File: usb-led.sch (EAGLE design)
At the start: 10 parts, among them U1 Tiny85-20-SMT

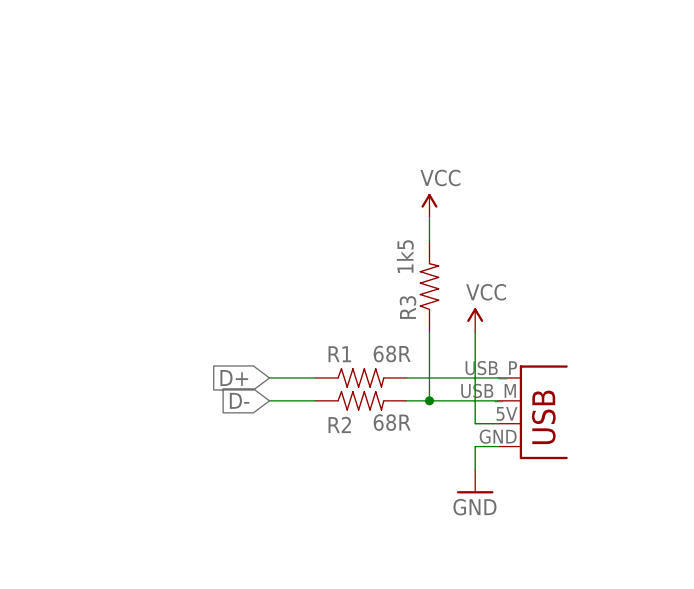
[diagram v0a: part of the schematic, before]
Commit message: Forgot two 3.6V Z-Diodes
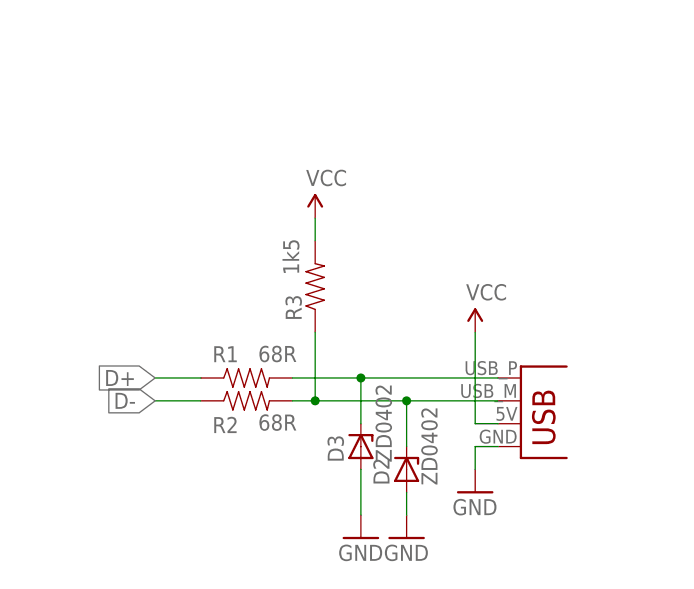
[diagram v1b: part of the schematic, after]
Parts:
- added D2, D3: ZD0402, z-diode-0402:ZD0402
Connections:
- net GND: now also D2.A, D3.A
- net N$1: now also D3.C
- net N$2: now also D2.C
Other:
- moved on the sheet: R1, R2, R3
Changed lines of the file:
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@@
 <part name="SUPPLY5" library="SparkFun-Aesthetics" deviceset="VCC" device=""/>
 <part name="R5" library="SparkFun-Passives" deviceset="RESISTOR" device="0402-RES" value="10K"/>
+<part name="D2" library="z-diode-0402" deviceset="ZD0402" device=""/>
+<part name="D3" library="z-diode-0402" deviceset="ZD0402" device=""/>
+<part name="GND4" library="SparkFun-Aesthetics" deviceset="GND" device=""/>
+<part name="GND5" library="SparkFun-Aesthetics" deviceset="GND" device=""/>
 </parts>
 <sheets>
@@
 <instance part="U1" gate="G$1" x="114.3" y="111.76"/>
 <instance part="FRAME1" gate="G$1" x="0" y="0"/>
-<instance part="R1" gate="G$1" x="129.54" y="53.34" smashed="yes">
-<attribute name="NAME" x="125.73" y="55.0926" size="1.778" layer="95"/>
-<attribute name="VALUE" x="130.81" y="55.118" size="1.778" layer="96"/>
+<instance part="R1" gate="G$1" x="116.84" y="53.34" smashed="yes">
+<attribute name="NAME" x="113.03" y="55.0926" size="1.778" layer="95"/>
+<attribute name="VALUE" x="118.11" y="55.118" size="1.778" layer="96"/>
 </instance>
-<instance part="R2" gate="G$1" x="129.54" y="50.8" smashed="yes">
-<attribute name="NAME" x="125.73" y="47.2186" size="1.778" layer="95"/>
-<attribute name="VALUE" x="130.81" y="47.498" size="1.778" layer="96"/>
+<instance part="R2" gate="G$1" x="116.84" y="50.8" smashed="yes">
+<attribute name="NAME" x="113.03" y="47.2186" size="1.778" layer="95"/>
+<attribute name="VALUE" x="118.11" y="47.498" size="1.778" layer="96"/>
 </instance>
-<instance part="R3" gate="G$1" x="137.16" y="63.5" smashed="yes" rot="R90">
-<attribute name="NAME" x="135.6614" y="59.69" size="1.778" layer="95" rot="R90"/>
-<attribute name="VALUE" x="135.382" y="64.77" size="1.778" layer="96" rot="R90"/>
+<instance part="R3" gate="G$1" x="124.46" y="63.5" smashed="yes" rot="R90">
+<attribute name="NAME" x="122.9614" y="59.69" size="1.778" layer="95" rot="R90"/>
+<attribute name="VALUE" x="122.682" y="64.77" size="1.778" layer="96" rot="R90"/>
 </instance>
 <instance part="SUPPLY1" gate="G$1" x="142.24" y="58.42"/>
@@
 <instance part="SUPPLY2" gate="G$1" x="93.98" y="121.92"/>
 <instance part="GND2" gate="1" x="93.98" y="101.6"/>
-<instance part="SUPPLY4" gate="G$1" x="137.16" y="71.12"/>
+<instance part="SUPPLY4" gate="G$1" x="124.46" y="71.12"/>
 <instance part="C1" gate="G$1" x="93.98" y="111.76"/>
 <instance part="GND3" gate="1" x="210.82" y="106.68"/>
@@
 <attribute name="VALUE" x="140.97" y="104.902" size="1.778" layer="96" rot="R180"/>
 </instance>
+<instance part="D2" gate="1" x="134.62" y="43.18" rot="R90"/>
+<instance part="D3" gate="1" x="129.54" y="45.72" rot="R90"/>
+<instance part="GND4" gate="1" x="134.62" y="35.56"/>
+<instance part="GND5" gate="1" x="129.54" y="35.56"/>
 </instances>
 <busses>
@@
 <pinref part="GND3" gate="1" pin="GND"/>
 </segment>
+<segment>
+<pinref part="D2" gate="1" pin="A"/>
+<wire x1="134.62" y1="40.64" x2="134.62" y2="38.1" width="0.1524" layer="91"/>
+<pinref part="GND4" gate="1" pin="GND"/>
+</segment>
+<segment>
+<pinref part="D3" gate="1" pin="A"/>
+<wire x1="129.54" y1="43.18" x2="129.54" y2="38.1" width="0.1524" layer="91"/>
+<pinref part="GND5" gate="1" pin="GND"/>
+</segment>
 </net>
 <net name="VCC" class="0">
@@
 <pinref part="R3" gate="G$1" pin="2"/>
 <pinref part="SUPPLY4" gate="G$1" pin="VCC"/>
-<wire x1="137.16" y1="71.12" x2="137.16" y2="68.58" width="0.1524" layer="91"/>
+<wire x1="124.46" y1="71.12" x2="124.46" y2="68.58" width="0.1524" layer="91"/>
 </segment>
 <segment>
@@
 <pinref part="R1" gate="G$1" pin="2"/>
 <pinref part="JP1" gate="G$1" pin="D+"/>
-<wire x1="134.62" y1="53.34" x2="144.78" y2="53.34" width="0.1524" layer="91"/>
+<wire x1="121.92" y1="53.34" x2="129.54" y2="53.34" width="0.1524" layer="91"/>
+<pinref part="D3" gate="1" pin="C"/>
+<wire x1="129.54" y1="53.34" x2="144.78" y2="53.34" width="0.1524" layer="91"/>
+<wire x1="129.54" y1="48.26" x2="129.54" y2="53.34" width="0.1524" layer="91"/>
+<junction x="129.54" y="53.34"/>
 </segment>
 </net>
@@
 <pinref part="JP1" gate="G$1" pin="D-"/>
 <pinref part="R2" gate="G$1" pin="2"/>
-<wire x1="144.78" y1="50.8" x2="137.16" y2="50.8" width="0.1524" layer="91"/>
+<wire x1="144.78" y1="50.8" x2="134.62" y2="50.8" width="0.1524" layer="91"/>
 <pinref part="R3" gate="G$1" pin="1"/>
-<wire x1="137.16" y1="50.8" x2="134.62" y2="50.8" width="0.1524" layer="91"/>
-<wire x1="137.16" y1="58.42" x2="137.16" y2="50.8" width="0.1524" layer="91"/>
-<junction x="137.16" y="50.8"/>
+<wire x1="134.62" y1="50.8" x2="124.46" y2="50.8" width="0.1524" layer="91"/>
+<wire x1="124.46" y1="50.8" x2="121.92" y2="50.8" width="0.1524" layer="91"/>
+<wire x1="124.46" y1="58.42" x2="124.46" y2="50.8" width="0.1524" layer="91"/>
+<junction x="124.46" y="50.8"/>
+<pinref part="D2" gate="1" pin="C"/>
+<wire x1="134.62" y1="45.72" x2="134.62" y2="50.8" width="0.1524" layer="91"/>
+<junction x="134.62" y="50.8"/>
 </segment>
 </net>
@@
 <segment>
 <pinref part="R2" gate="G$1" pin="1"/>
-<wire x1="124.46" y1="50.8" x2="119.38" y2="50.8" width="0.1524" layer="91"/>
-<label x="119.38" y="50.8" size="1.778" layer="95" rot="R180" xref="yes"/>
+<wire x1="111.76" y1="50.8" x2="106.68" y2="50.8" width="0.1524" layer="91"/>
+<label x="106.68" y="50.8" size="1.778" layer="95" rot="R180" xref="yes"/>
 </segment>
 <segment>
@@
 <segment>
 <pinref part="R1" gate="G$1" pin="1"/>
-<wire x1="124.46" y1="53.34" x2="119.38" y2="53.34" width="0.1524" layer="91"/>
-<label x="119.38" y="53.34" size="1.778" layer="95" rot="R180" xref="yes"/>
+<wire x1="111.76" y1="53.34" x2="106.68" y2="53.34" width="0.1524" layer="91"/>
+<label x="106.68" y="53.34" size="1.778" layer="95" rot="R180" xref="yes"/>
 </segment>
 <segment>

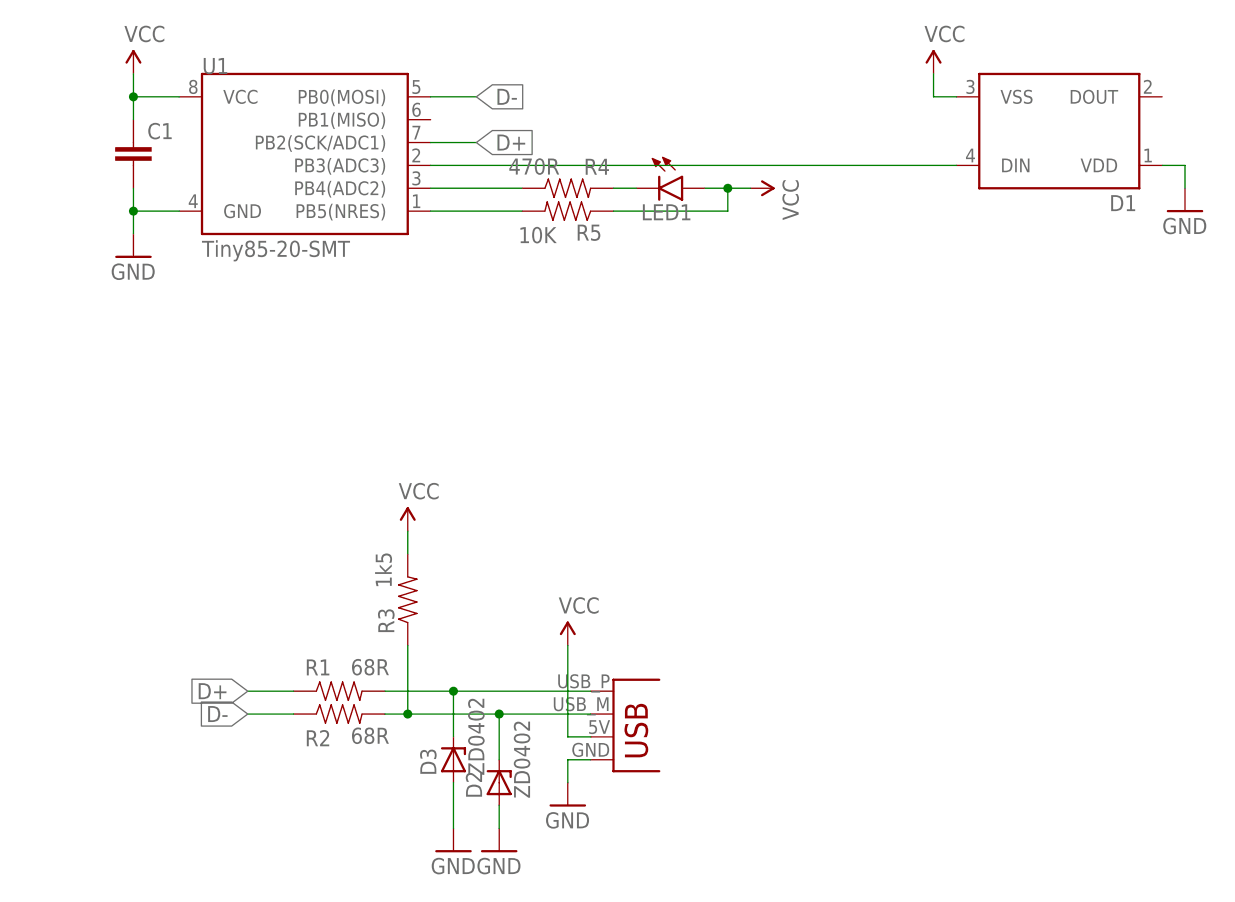
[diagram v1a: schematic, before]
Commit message: Use real USB connector, not PCB-trace-based one
OSHPark PCBs are not thick enoguh (1.5mm, not 2.4mm)
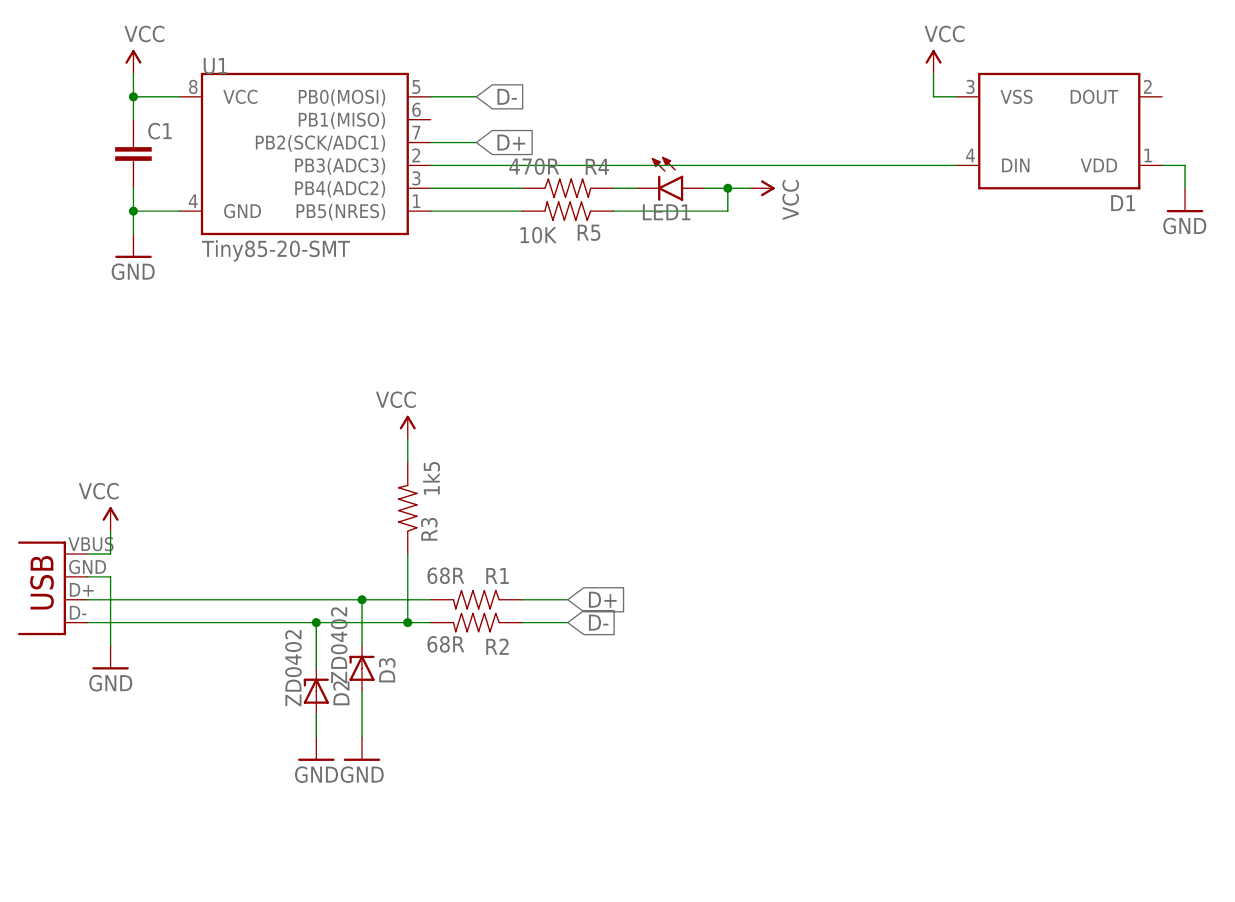
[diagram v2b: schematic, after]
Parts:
- removed JP1: USBPCB, SparkFun-Connectors:USBPCB
- added JP2: USB-A-H, SparkFun-Connectors:USB-A-H
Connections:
- net GND: now also JP2.VBUS; no longer JP1.GND
- net N$1: now also JP2.D-; no longer JP1.D+
- net N$2: now also JP2.D+; no longer JP1.D-
- net VCC: now also JP2.GND; no longer JP1.VBUS
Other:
- moved on the sheet: D2, D3, R1, R2, R3
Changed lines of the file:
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@@
 <?xml version="1.0" encoding="utf-8"?>
 <!DOCTYPE eagle SYSTEM "eagle.dtd">
-<eagle version="6.5.0">
+<eagle version="6.6.0">
 <drawing>
 <settings>
@@
 </classes>
 <parts>
-<part name="JP1" library="SparkFun-Connectors" deviceset="USB" device="PCB"/>
 <part name="U1" library="SparkFun-DigitalIC" deviceset="ATTINY45" device="TINY85-20-SMT" value="Tiny85-20-SMT"/>
 <part name="FRAME1" library="SparkFun-Aesthetics" deviceset="FRAME-A4L" device=""/>
@@
 <part name="R2" library="SparkFun-Passives" deviceset="RESISTOR" device="0402-RES" value="68R"/>
 <part name="R3" library="SparkFun-Passives" deviceset="RESISTOR" device="0402-RES" value="1k5"/>
-<part name="SUPPLY1" library="SparkFun-Aesthetics" deviceset="VCC" device=""/>
-<part name="GND1" library="SparkFun-Aesthetics" deviceset="GND" device=""/>
 <part name="SUPPLY2" library="SparkFun-Aesthetics" deviceset="VCC" device=""/>
 <part name="GND2" library="SparkFun-Aesthetics" deviceset="GND" device=""/>
@@
 <part name="GND4" library="SparkFun-Aesthetics" deviceset="GND" device=""/>
 <part name="GND5" library="SparkFun-Aesthetics" deviceset="GND" device=""/>
+<part name="JP2" library="SparkFun-Connectors" deviceset="USB" device="-A-H"/>
+<part name="SUPPLY6" library="SparkFun-Aesthetics" deviceset="VCC" device=""/>
+<part name="GND6" library="SparkFun-Aesthetics" deviceset="GND" device=""/>
 </parts>
 <sheets>
@@
 </plain>
 <instances>
-<instance part="JP1" gate="G$1" x="147.32" y="45.72"/>
 <instance part="U1" gate="G$1" x="114.3" y="111.76"/>
 <instance part="FRAME1" gate="G$1" x="0" y="0"/>
-<instance part="R1" gate="G$1" x="116.84" y="53.34" smashed="yes">
-<attribute name="NAME" x="113.03" y="55.0926" size="1.778" layer="95"/>
-<attribute name="VALUE" x="118.11" y="55.118" size="1.778" layer="96"/>
-</instance>
-<instance part="R2" gate="G$1" x="116.84" y="50.8" smashed="yes">
-<attribute name="NAME" x="113.03" y="47.2186" size="1.778" layer="95"/>
-<attribute name="VALUE" x="118.11" y="47.498" size="1.778" layer="96"/>
-</instance>
-<instance part="R3" gate="G$1" x="124.46" y="63.5" smashed="yes" rot="R90">
-<attribute name="NAME" x="122.9614" y="59.69" size="1.778" layer="95" rot="R90"/>
-<attribute name="VALUE" x="122.682" y="64.77" size="1.778" layer="96" rot="R90"/>
-</instance>
-<instance part="SUPPLY1" gate="G$1" x="142.24" y="58.42"/>
-<instance part="GND1" gate="1" x="142.24" y="40.64"/>
+<instance part="R1" gate="G$1" x="132.08" y="63.5" smashed="yes" rot="MR0">
+<attribute name="NAME" x="135.89" y="65.2526" size="1.778" layer="95" rot="MR0"/>
+<attribute name="VALUE" x="130.81" y="65.278" size="1.778" layer="96" rot="MR0"/>
+</instance>
+<instance part="R2" gate="G$1" x="132.08" y="60.96" smashed="yes" rot="MR0">
+<attribute name="NAME" x="135.89" y="57.3786" size="1.778" layer="95" rot="MR0"/>
+<attribute name="VALUE" x="130.81" y="57.658" size="1.778" layer="96" rot="MR0"/>
+</instance>
+<instance part="R3" gate="G$1" x="124.46" y="73.66" smashed="yes" rot="MR90">
+<attribute name="NAME" x="125.9586" y="69.85" size="1.778" layer="95" rot="MR90"/>
+<attribute name="VALUE" x="126.238" y="74.93" size="1.778" layer="96" rot="MR90"/>
+</instance>
 <instance part="SUPPLY2" gate="G$1" x="93.98" y="121.92"/>
 <instance part="GND2" gate="1" x="93.98" y="101.6"/>
-<instance part="SUPPLY4" gate="G$1" x="124.46" y="71.12"/>
+<instance part="SUPPLY4" gate="G$1" x="124.46" y="81.28" rot="MR0"/>
 <instance part="C1" gate="G$1" x="93.98" y="111.76"/>
 <instance part="GND3" gate="1" x="210.82" y="106.68"/>
@@
 <attribute name="VALUE" x="140.97" y="104.902" size="1.778" layer="96" rot="R180"/>
 </instance>
-<instance part="D2" gate="1" x="134.62" y="43.18" rot="R90"/>
-<instance part="D3" gate="1" x="129.54" y="45.72" rot="R90"/>
-<instance part="GND4" gate="1" x="134.62" y="35.56"/>
-<instance part="GND5" gate="1" x="129.54" y="35.56"/>
+<instance part="D2" gate="1" x="114.3" y="53.34" rot="MR90"/>
+<instance part="D3" gate="1" x="119.38" y="55.88" rot="MR90"/>
+<instance part="GND4" gate="1" x="114.3" y="45.72" rot="MR0"/>
+<instance part="GND5" gate="1" x="119.38" y="45.72" rot="MR0"/>
+<instance part="JP2" gate="G$1" x="86.36" y="68.58" rot="R180"/>
+<instance part="SUPPLY6" gate="G$1" x="91.44" y="71.12" rot="MR0"/>
+<instance part="GND6" gate="1" x="91.44" y="55.88" rot="MR0"/>
 </instances>
 <busses>
@@
 <nets>
 <net name="GND" class="0">
-<segment>
-<pinref part="GND1" gate="1" pin="GND"/>
-<pinref part="JP1" gate="G$1" pin="GND"/>
-<wire x1="142.24" y1="43.18" x2="142.24" y2="45.72" width="0.1524" layer="91"/>
-<wire x1="142.24" y1="45.72" x2="144.78" y2="45.72" width="0.1524" layer="91"/>
-</segment>
 <segment>
 <pinref part="U1" gate="G$1" pin="GND"/>
@@
 <segment>
 <pinref part="D2" gate="1" pin="A"/>
-<wire x1="134.62" y1="40.64" x2="134.62" y2="38.1" width="0.1524" layer="91"/>
+<wire x1="114.3" y1="50.8" x2="114.3" y2="48.26" width="0.1524" layer="91"/>
 <pinref part="GND4" gate="1" pin="GND"/>
 </segment>
 <segment>
 <pinref part="D3" gate="1" pin="A"/>
-<wire x1="129.54" y1="43.18" x2="129.54" y2="38.1" width="0.1524" layer="91"/>
+<wire x1="119.38" y1="53.34" x2="119.38" y2="48.26" width="0.1524" layer="91"/>
 <pinref part="GND5" gate="1" pin="GND"/>
 </segment>
+<segment>
+<pinref part="JP2" gate="G$1" pin="VBUS"/>
+<wire x1="88.9" y1="66.04" x2="91.44" y2="66.04" width="0.1524" layer="91"/>
+<wire x1="91.44" y1="66.04" x2="91.44" y2="58.42" width="0.1524" layer="91"/>
+<pinref part="GND6" gate="1" pin="GND"/>
+</segment>
 </net>
 <net name="VCC" class="0">
-<segment>
-<pinref part="JP1" gate="G$1" pin="VBUS"/>
-<pinref part="SUPPLY1" gate="G$1" pin="VCC"/>
-<wire x1="144.78" y1="48.26" x2="142.24" y2="48.26" width="0.1524" layer="91"/>
-<wire x1="142.24" y1="48.26" x2="142.24" y2="58.42" width="0.1524" layer="91"/>
-</segment>
 <segment>
 <pinref part="U1" gate="G$1" pin="VCC"/>
@@
 <pinref part="R3" gate="G$1" pin="2"/>
 <pinref part="SUPPLY4" gate="G$1" pin="VCC"/>
-<wire x1="124.46" y1="71.12" x2="124.46" y2="68.58" width="0.1524" layer="91"/>
+<wire x1="124.46" y1="81.28" x2="124.46" y2="78.74" width="0.1524" layer="91"/>
 </segment>
 <segment>
@@
 <junction x="160.02" y="109.22"/>
 </segment>
-</net>
-<net name="N$1" class="0">
-<segment>
-<pinref part="R1" gate="G$1" pin="2"/>
-<pinref part="JP1" gate="G$1" pin="D+"/>
-<wire x1="121.92" y1="53.34" x2="129.54" y2="53.34" width="0.1524" layer="91"/>
-<pinref part="D3" gate="1" pin="C"/>
-<wire x1="129.54" y1="53.34" x2="144.78" y2="53.34" width="0.1524" layer="91"/>
-<wire x1="129.54" y1="48.26" x2="129.54" y2="53.34" width="0.1524" layer="91"/>
-<junction x="129.54" y="53.34"/>
+<segment>
+<pinref part="JP2" gate="G$1" pin="GND"/>
+<wire x1="88.9" y1="68.58" x2="91.44" y2="68.58" width="0.1524" layer="91"/>
+<wire x1="91.44" y1="68.58" x2="91.44" y2="71.12" width="0.1524" layer="91"/>
+<pinref part="SUPPLY6" gate="G$1" pin="VCC"/>
 </segment>
 </net>
 <net name="N$2" class="0">
 <segment>
-<pinref part="JP1" gate="G$1" pin="D-"/>
 <pinref part="R2" gate="G$1" pin="2"/>
-<wire x1="144.78" y1="50.8" x2="134.62" y2="50.8" width="0.1524" layer="91"/>
 <pinref part="R3" gate="G$1" pin="1"/>
-<wire x1="134.62" y1="50.8" x2="124.46" y2="50.8" width="0.1524" layer="91"/>
-<wire x1="124.46" y1="50.8" x2="121.92" y2="50.8" width="0.1524" layer="91"/>
-<wire x1="124.46" y1="58.42" x2="124.46" y2="50.8" width="0.1524" layer="91"/>
-<junction x="124.46" y="50.8"/>
+<wire x1="114.3" y1="60.96" x2="124.46" y2="60.96" width="0.1524" layer="91"/>
+<wire x1="124.46" y1="60.96" x2="127" y2="60.96" width="0.1524" layer="91"/>
+<wire x1="124.46" y1="68.58" x2="124.46" y2="60.96" width="0.1524" layer="91"/>
+<junction x="124.46" y="60.96"/>
 <pinref part="D2" gate="1" pin="C"/>
-<wire x1="134.62" y1="45.72" x2="134.62" y2="50.8" width="0.1524" layer="91"/>
-<junction x="134.62" y="50.8"/>
+<wire x1="114.3" y1="55.88" x2="114.3" y2="60.96" width="0.1524" layer="91"/>
+<junction x="114.3" y="60.96"/>
+<wire x1="114.3" y1="60.96" x2="91.44" y2="60.96" width="0.1524" layer="91"/>
+</segment>
+<segment>
+<pinref part="JP2" gate="G$1" pin="D+"/>
+<wire x1="88.9" y1="60.96" x2="91.44" y2="60.96" width="0.1524" layer="91"/>
 </segment>
 </net>
@@
 <segment>
 <pinref part="R2" gate="G$1" pin="1"/>
-<wire x1="111.76" y1="50.8" x2="106.68" y2="50.8" width="0.1524" layer="91"/>
-<label x="106.68" y="50.8" size="1.778" layer="95" rot="R180" xref="yes"/>
+<wire x1="137.16" y1="60.96" x2="142.24" y2="60.96" width="0.1524" layer="91"/>
+<label x="142.24" y="60.96" size="1.778" layer="95" rot="MR180" xref="yes"/>
 </segment>
 <segment>
@@
 <segment>
 <pinref part="R1" gate="G$1" pin="1"/>
-<wire x1="111.76" y1="53.34" x2="106.68" y2="53.34" width="0.1524" layer="91"/>
-<label x="106.68" y="53.34" size="1.778" layer="95" rot="R180" xref="yes"/>
+<wire x1="137.16" y1="63.5" x2="142.24" y2="63.5" width="0.1524" layer="91"/>
+<label x="142.24" y="63.5" size="1.778" layer="95" rot="MR180" xref="yes"/>
 </segment>
 <segment>
@@
 </segment>
 </net>
+<net name="N$1" class="0">
+<segment>
+<pinref part="JP2" gate="G$1" pin="D-"/>
+<pinref part="R1" gate="G$1" pin="2"/>
+<wire x1="127" y1="63.5" x2="119.38" y2="63.5" width="0.1524" layer="91"/>
+<pinref part="D3" gate="1" pin="C"/>
+<wire x1="119.38" y1="58.42" x2="119.38" y2="63.5" width="0.1524" layer="91"/>
+<junction x="119.38" y="63.5"/>
+<wire x1="88.9" y1="63.5" x2="119.38" y2="63.5" width="0.1524" layer="91"/>
+</segment>
+</net>
